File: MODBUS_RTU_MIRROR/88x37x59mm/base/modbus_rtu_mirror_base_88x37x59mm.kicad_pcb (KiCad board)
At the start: 2 copper layers, 82 x 31 mm, 12 parts, among them J1 Conn_01x01_Male, J2 Conn_01x02_Female, J3 Conn_01x02_Female, J4 Conn_01x02_Female, J5 Conn_01x02_Female, U1 ST485EBDR, U2 ST485EBDR

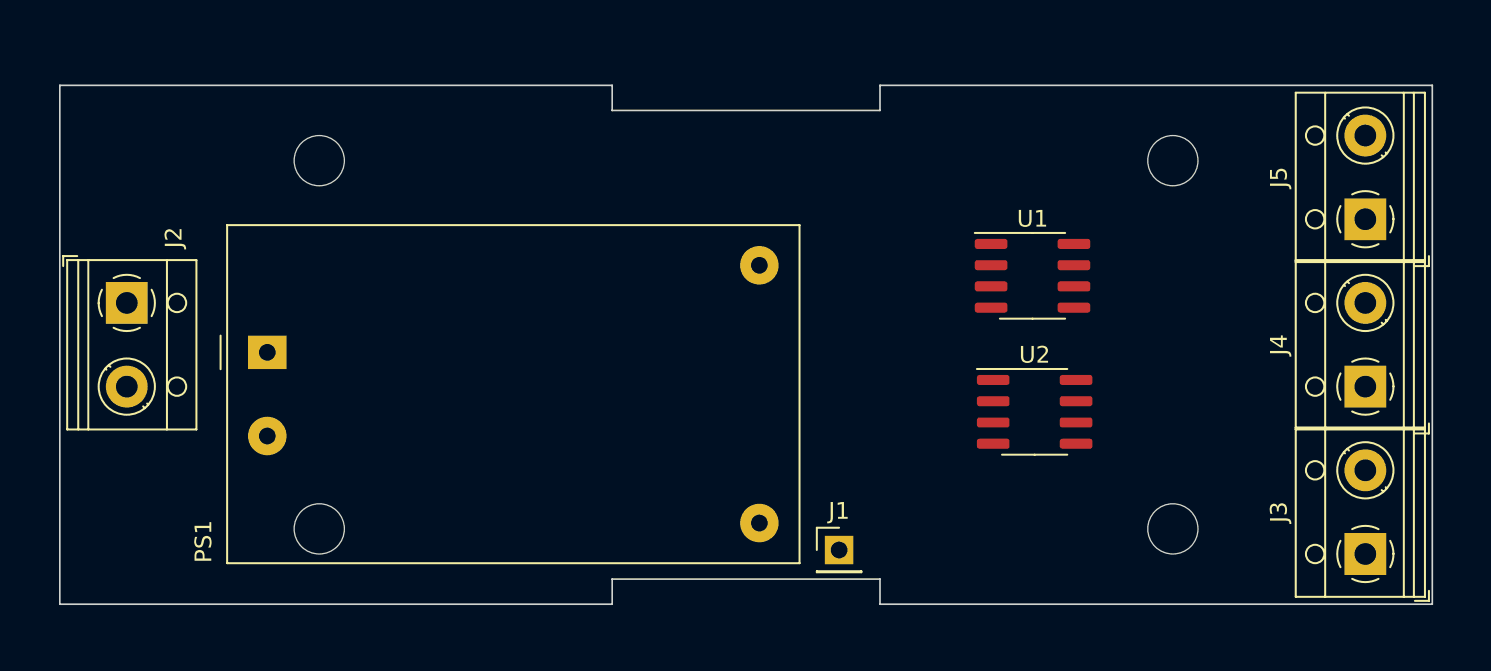
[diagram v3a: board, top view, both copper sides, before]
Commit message: all traces routed
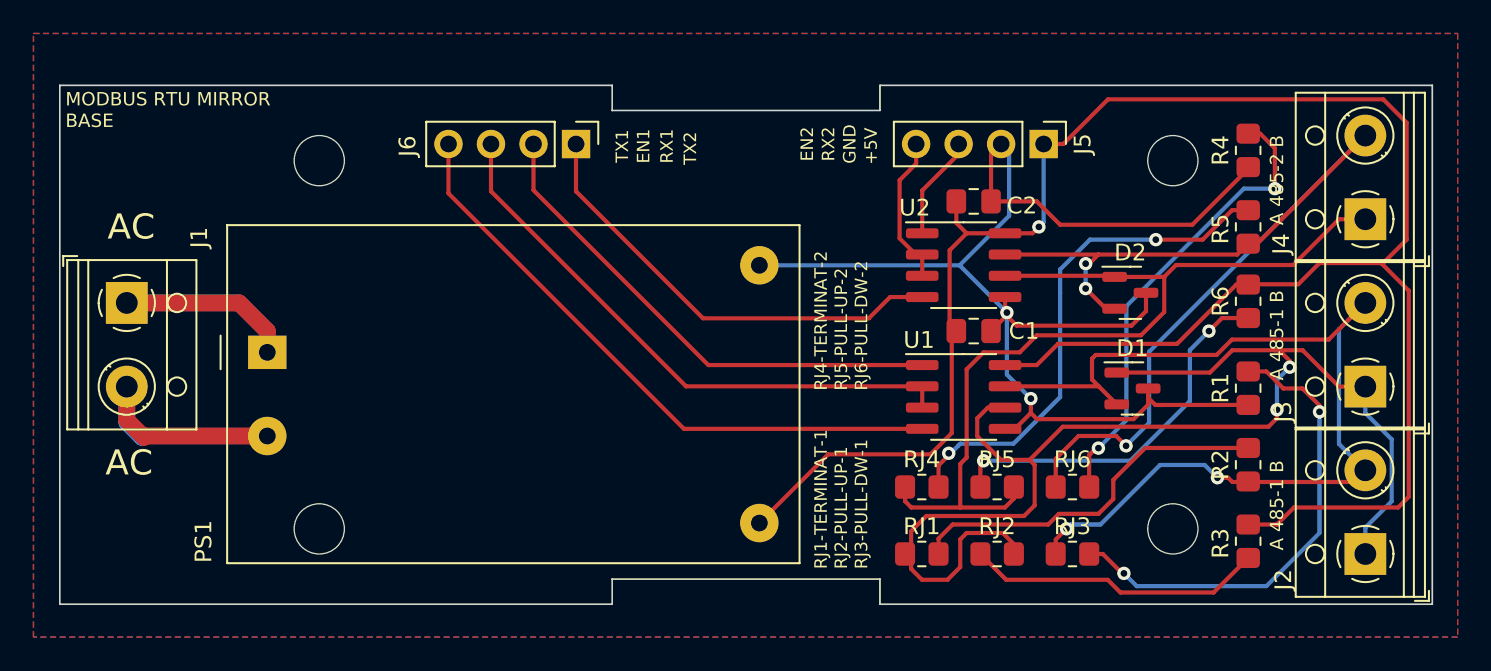
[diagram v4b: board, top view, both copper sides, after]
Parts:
- removed the J1 at (146.6, 127.8)
- added C1: C, Capacitor_SMD:C_0805_2012Metric_Pad1.18x1.45mm_HandSolder, F.Cu at (154.6, 114.7)
- added C2: C, Capacitor_SMD:C_0805_2012Metric_Pad1.18x1.45mm_HandSolder, F.Cu at (154.6, 106.9)
- added D1: SM712_SOT23, Package_TO_SOT_SMD:SOT-23, F.Cu at (164.1, 118.1)
- added D2: SM712_SOT23, Package_TO_SOT_SMD:SOT-23, F.Cu at (164.0, 112.4)
- added J5: Conn_01x04_Male, Connector_PinHeader_2.54mm:PinHeader_1x04_P2.54mm_Vertical, F.Cu at (158.8, 103.5)
- added J6: Conn_01x04_Male, Connector_PinHeader_2.54mm:PinHeader_1x04_P2.54mm_Vertical, F.Cu at (130.8, 103.5)
- added R1: 4.7k, Resistor_SMD:R_0805_2012Metric_Pad1.20x1.40mm_HandSolder, F.Cu at (171.0, 118.1)
- added R2: 120, Resistor_SMD:R_0805_2012Metric_Pad1.20x1.40mm_HandSolder, F.Cu at (171.0, 122.7)
- added R3: 4.7k, Resistor_SMD:R_0805_2012Metric_Pad1.20x1.40mm_HandSolder, F.Cu at (171.0, 127.2)
- added R4: 4.7k, Resistor_SMD:R_0805_2012Metric_Pad1.20x1.40mm_HandSolder, F.Cu at (171.0, 103.9)
- added R5: 120, Resistor_SMD:R_0805_2012Metric_Pad1.20x1.40mm_HandSolder, F.Cu at (171.0, 108.5)
- added R6: 4.7k, Resistor_SMD:R_0805_2012Metric_Pad1.20x1.40mm_HandSolder, F.Cu at (171.0, 112.9)
- added RJ1: 0, Resistor_SMD:R_0805_2012Metric_Pad1.20x1.40mm_HandSolder, F.Cu at (151.5, 128.0)
- added RJ2: 0, Resistor_SMD:R_0805_2012Metric_Pad1.20x1.40mm_HandSolder, F.Cu at (156.0, 128.0)
- added RJ3: 0, Resistor_SMD:R_0805_2012Metric_Pad1.20x1.40mm_HandSolder, F.Cu at (160.5, 128.0)
- added RJ4: 0, Resistor_SMD:R_0805_2012Metric_Pad1.20x1.40mm_HandSolder, F.Cu at (151.5, 124.0)
- added RJ5: 0, Resistor_SMD:R_0805_2012Metric_Pad1.20x1.40mm_HandSolder, F.Cu at (156.0, 124.0)
- added RJ6: 0, Resistor_SMD:R_0805_2012Metric_Pad1.20x1.40mm_HandSolder, F.Cu at (160.5, 124.0)
- moved U1 4.33 mm to (154.0, 118.6)
- moved U2 4.16 mm to (154.0, 110.7)
- renumbered J2 to J1, J3 to J2, J4 to J3, J5 to J4, REF** to MH00, REF** to MH01, REF** to MH02, REF** to MH03, U2 to U1, U1 to U2
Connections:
- J1 pad 1: unconnected-(J2-Pad1) -> Net-(PS1-Pad1)
- J1 pad 2: unconnected-(J2-Pad2) -> Net-(PS1-Pad2)
- J2 pad 1: unconnected-(J3-Pad1) -> /RS485_1_A
- J2 pad 2: unconnected-(J3-Pad2) -> /RS485_1_B
- J3 pad 1: unconnected-(J4-Pad1) -> /RS485_1_A
- J3 pad 2: unconnected-(J4-Pad2) -> /RS485_1_B
- J4 pad 1: unconnected-(J5-Pad1) -> /RS485_2_A
- J4 pad 2: unconnected-(J5-Pad2) -> /RS485_2_B
- PS1 pad 1: unconnected-(PS1-Pad1) -> Net-(PS1-Pad1)
- PS1 pad 2: unconnected-(PS1-Pad2) -> Net-(PS1-Pad2)
- PS1 pad 3: unconnected-(PS1-Pad3) -> GND
- PS1 pad 4: unconnected-(PS1-Pad4) -> +5V
- U1 pad 1: unconnected-(U2-Pad1) -> Net-(J6-Pad2)
- U1 pad 2: unconnected-(U2-Pad2) -> Net-(J6-Pad3)
- U1 pad 3: unconnected-(U2-Pad3) -> Net-(J6-Pad3)
- U1 pad 4: unconnected-(U2-Pad4) -> Net-(J6-Pad4)
- U1 pad 5: unconnected-(U2-Pad5) -> GND
- U1 pad 6: unconnected-(U2-Pad6) -> /RS485_1_A
- U1 pad 7: unconnected-(U2-Pad7) -> /RS485_1_B
- U1 pad 8: unconnected-(U2-Pad8) -> +5V
- U2 pad 1: unconnected-(U1-Pad1) -> Net-(U2-Pad1)
- U2 pad 2: unconnected-(U1-Pad2) -> Net-(U2-Pad3)
- U2 pad 3: unconnected-(U1-Pad3) -> Net-(U2-Pad3)
- U2 pad 4: unconnected-(U1-Pad4) -> Net-(U2-Pad4)
- U2 pad 5: unconnected-(U1-Pad5) -> GND
- U2 pad 6: unconnected-(U1-Pad6) -> /RS485_2_A
- U2 pad 7: unconnected-(U1-Pad7) -> /RS485_2_B
- U2 pad 8: unconnected-(U1-Pad8) -> +5V
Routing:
- net +5V: track 0.00 -> 120.3 mm, vias 0 -> 1
- net GND: track 0.00 -> 81.5 mm, vias 0 -> 2
- net /RS485_1_A: track 0.00 -> 77.9 mm, vias 0 -> 2
- net /RS485_2_B: track 0.00 -> 60.3 mm, vias 0 -> 3
- net /RS485_1_B: track 0.00 -> 59.9 mm, vias 0 -> 2
- net /RS485_2_A: track 0.00 -> 55.1 mm
- net Net-(J6-Pad4): track 0.00 -> 37.1 mm
- net Net-(J6-Pad3): track 0.00 -> 34.7 mm
- net Net-(R5-Pad1): track 0.00 -> 30.6 mm, vias 0 -> 2
- net Net-(J6-Pad2): track 0.00 -> 30.3 mm
- net Net-(R1-Pad1): track 0.00 -> 28.6 mm, vias 0 -> 2
- net Net-(R4-Pad1): track 0.00 -> 28.0 mm, vias 0 -> 2
- net Net-(U2-Pad4): track 0.00 -> 27.2 mm
- net Net-(R6-Pad2): track 0.00 -> 22.8 mm, vias 0 -> 2
- net Net-(RJ1-Pad2): track 0.00 -> 22.3 mm
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- added copper zone on B.Cu, net GND
- added copper zone on F.Cu, net GND
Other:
- board text added: "+5V"
- board text added: "A 485-1 B"
- board text added: "A 485-2 B"
- board text added: "AC"
- board text added: "EN1"
- board text added: "EN2"
- board text added: "GND"
- board text added: "MODBUS RTU MIRROR BASE"
- board text added: "RJ1-TERMINAT-1 RJ2-PULL-UP-1 RJ3-PULL-DW-1"
- board text added: "RJ4-TERMINAT-2 RJ5-PULL-UP-2 RJ6-PULL-DW-2"
- board text added: "RX1"
- board text added: "RX2"
- board text added: "TX1"
- board text added: "TX2"
